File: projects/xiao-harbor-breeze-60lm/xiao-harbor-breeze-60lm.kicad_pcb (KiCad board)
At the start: 2 copper layers, 27.2 x 44.5 mm, 17 parts, among them CN1 XY122V-5.08-2P, CN2 XY122V-5.08-2P, J1 1165SDIG-07, J2 1165SDIG-07, U1 BQ25185DLHR, U2 ME6210A33PG

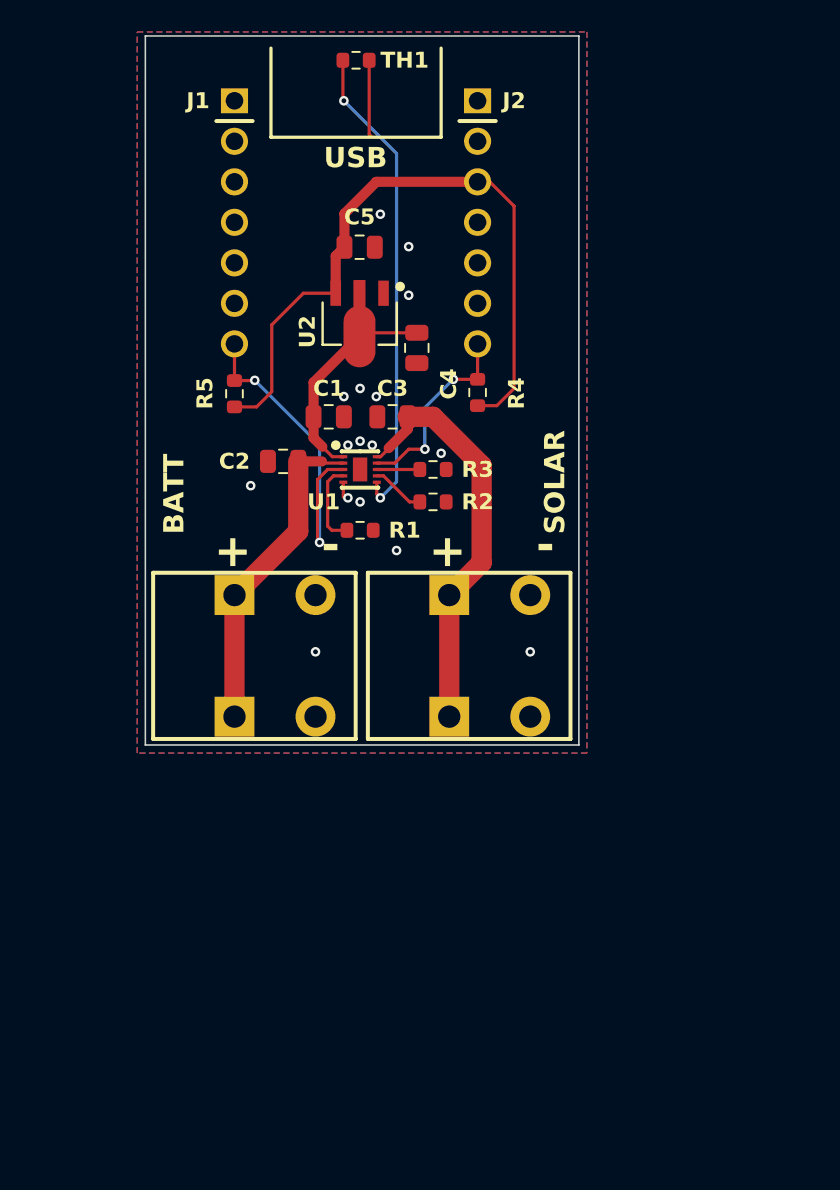
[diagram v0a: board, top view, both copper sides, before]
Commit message: Add low voltage and over voltage protection
This part is a final safety net for battery charage management.

It is configured to have a low voltage cutoff of 2.5V and an over
voltage cutoff of 4.3V.

These values are comfortably outside the range of the change controller
thresholds, but still within the ranges generally accepted to avoid
permanent cell damage.

If for some reason we over charge or over discharge, this part will do a
low side disconnect of the battery from the rest of the system.

lib: Add simple logos

Currently unused, but are available.

See:
  * https://meshtastic.org/docs/legal/licensing-and-trademark/#community-project-logos-m-powered--m-pwrd
  * https://oshwa.org/resources/open-source-hardware-logo/
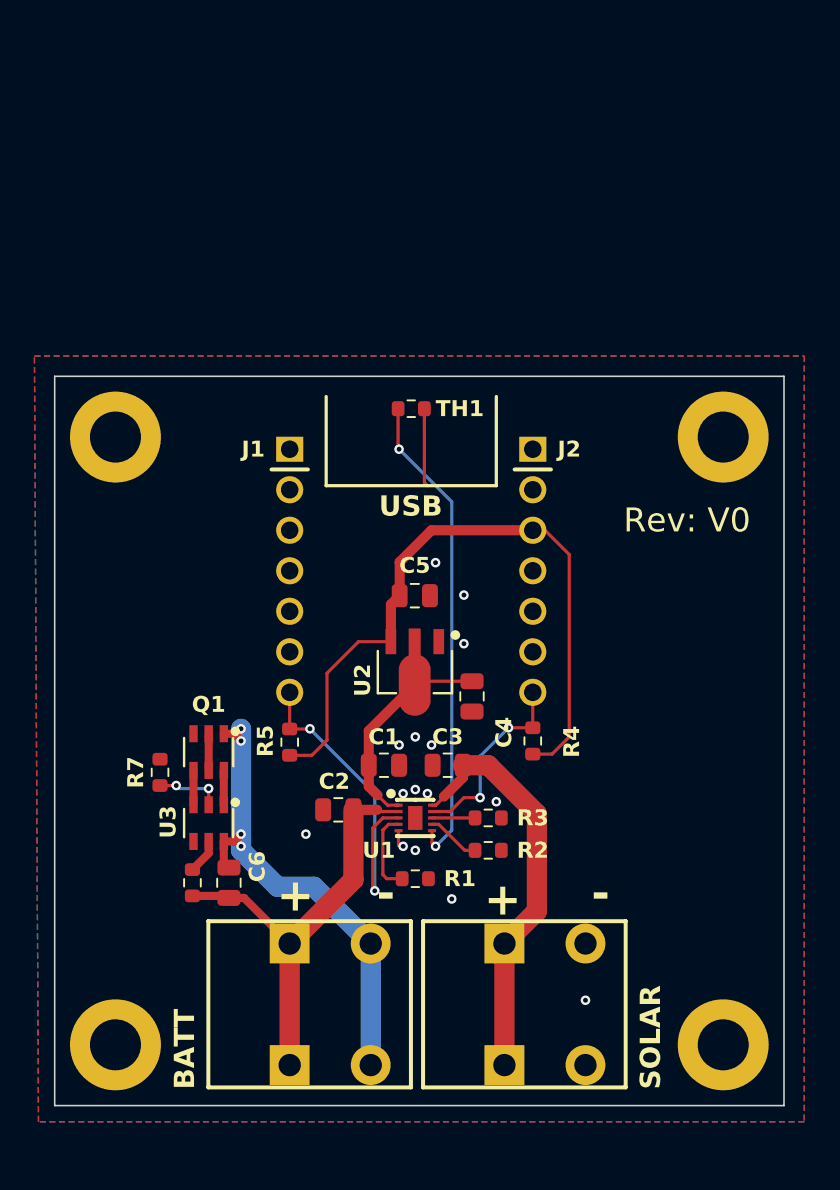
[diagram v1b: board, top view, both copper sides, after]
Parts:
- added C6: 22uF, Capacitor_SMD:C_0805_2012Metric, F.Cu at (136.8, 104.9)
- added H1: MountingHole_Pad, MountingHole:MountingHole_3.2mm_M3_ISO7380_Pad, F.Cu at (167.8, 115.1)
- added H2: MountingHole_Pad, MountingHole:MountingHole_3.2mm_M3_ISO7380_Pad, F.Cu at (129.7, 115.1)
- added H3: MountingHole_Pad, MountingHole:MountingHole_3.2mm_M3_ISO7380_Pad, F.Cu at (167.8, 77.0)
- added H4: MountingHole_Pad, MountingHole:MountingHole_3.2mm_M3_ISO7380_Pad, F.Cu at (129.7, 77.0)
- added Q1: UMW8205A, easyeda2kicad:SOT-23-6_L2.9-W1.6-P0.95-LS2.8-BL, F.Cu at (135.5, 96.7)
- added R6: 100, Resistor_SMD:R_0603_1608Metric, F.Cu at (134.5, 104.9)
- added R7: 1K, Resistor_SMD:R_0603_1608Metric, F.Cu at (132.5, 98.0)
- added U3: DW01A_C351410, easyeda2kicad:SOT-23-6_L2.9-W1.6-P0.95-LS2.8-BL, F.Cu at (135.5, 101.2)
- moved CN2 22.1 mm to (143.2, 112.5)
- moved C1 22.1 mm to (146.5, 97.5)
- moved C3 22.1 mm to (150.5, 97.5)
- moved C4 22.1 mm to (152.1, 93.2)
- moved CN1 22.1 mm to (156.6, 112.5)
- moved R2 22.1 mm to (153.1, 102.9)
- moved C2 22.1 mm to (143.7, 100.3)
- moved C5 22.1 mm to (148.5, 86.9)
- moved J1 22.1 mm to (140.6, 85.3)
- moved J2 22.1 mm to (155.9, 85.3)
- moved R1 22.1 mm to (148.5, 104.6)
- moved R3 22.1 mm to (153.1, 100.8)
- moved R4 22.1 mm to (155.9, 96.0)
- moved R5 22.1 mm to (140.6, 96.1)
- moved TH1 22.1 mm to (148.2, 75.2)
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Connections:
- CN2 pad 2: GND -> -BATT
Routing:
- net -BATT: track 0.00 -> 31.5 mm, vias 0 -> 4
- net +BATT: track 20.5 -> 27.9 mm
- net Net-(U3-VM): track 0.00 -> 4.14 mm, vias 0 -> 2
- net Net-(Q1-D1/D2-Pad2): track 0.00 -> 2.30 mm
- net Net-(U3-VCC): track 0.00 -> 2.18 mm
- net Net-(Q1-G2): track 0.00 -> 2.15 mm
- net Net-(Q1-G1): track 0.00 -> 2.15 mm
- net GND: vias 16 -> 15
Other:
- board size 27.2 x 44.5 mm -> 45.7 x 45.7 mm
- board text added: "Rev: V0"
- board text added: "flyovermesh.org"
- board text added: "github.com/kelledge/heliomesh"

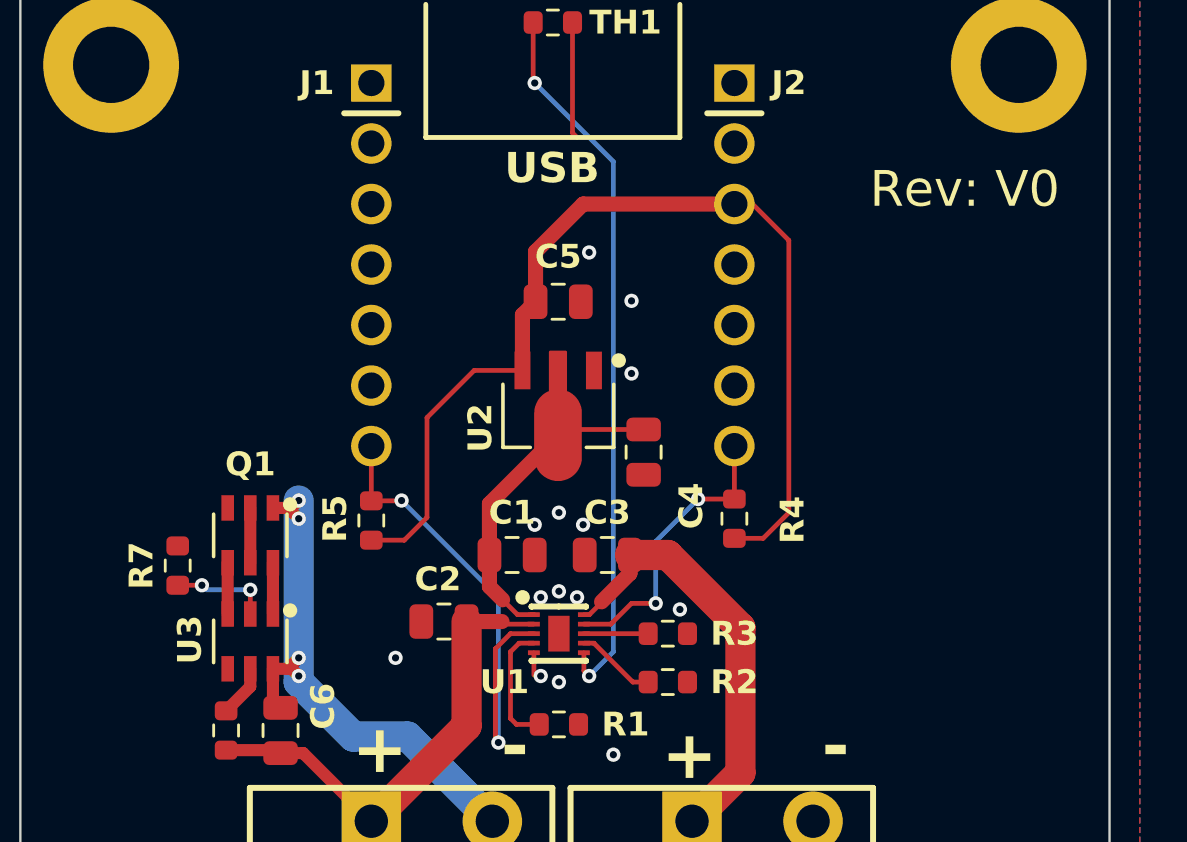
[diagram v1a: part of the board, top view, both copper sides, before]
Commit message: Add ziptie mounting slots
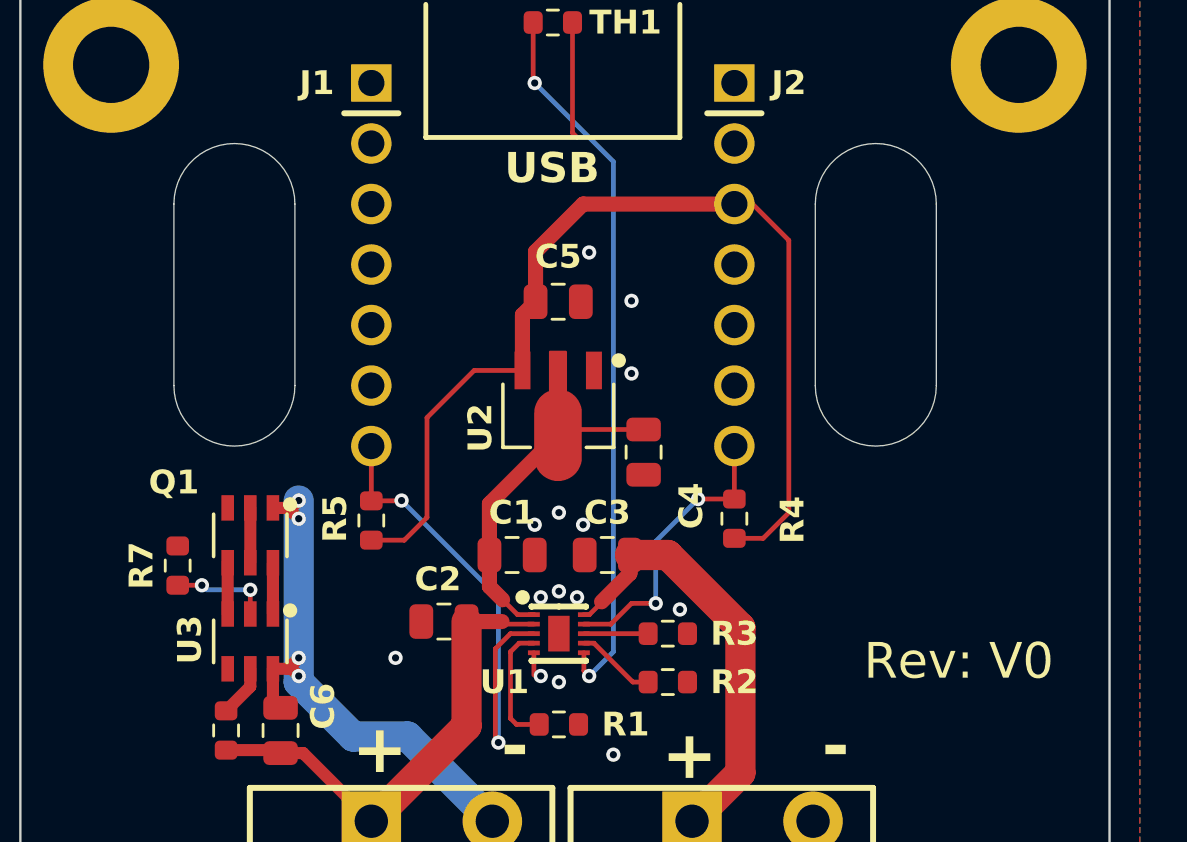
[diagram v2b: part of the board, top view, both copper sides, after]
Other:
- outline, holes or cut-outs redrawn
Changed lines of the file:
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@@
 		(at 135.540862 96.711 180)
 		(property "Reference" "Q1"
-			(at 0 2.985 0)
+			(at 3.206862 2.223 0)
 			(layer "F.SilkS")
 			(effects
@@
 		(layer "F.SilkS")
 	)
+	(gr_line
+		(start 132.334 82.804)
+		(end 132.334 90.424)
+		(stroke
+			(width 0.05)
+			(type default)
+		)
+		(layer "Edge.Cuts")
+	)
+	(gr_line
+		(start 164.338 82.804)
+		(end 164.338 90.424)
+		(stroke
+			(width 0.05)
+			(type default)
+		)
+		(layer "Edge.Cuts")
+	)
+	(gr_arc
+		(start 132.334 82.804)
+		(mid 134.874 80.264)
+		(end 137.414 82.804)
+		(stroke
+			(width 0.05)
+			(type default)
+		)
+		(layer "Edge.Cuts")
+	)
 	(gr_rect
 		(start 125.888862 73.152)
@@
 		(layer "Edge.Cuts")
 	)
+	(gr_arc
+		(start 159.258 82.804)
+		(mid 161.798 80.264)
+		(end 164.338 82.804)
+		(stroke
+			(width 0.05)
+			(type default)
+		)
+		(layer "Edge.Cuts")
+	)
+	(gr_line
+		(start 137.414 82.804)
+		(end 137.414 90.424)
+		(stroke
+			(width 0.05)
+			(type default)
+		)
+		(layer "Edge.Cuts")
+	)
+	(gr_line
+		(start 159.258 82.804)
+		(end 159.258 90.424)
+		(stroke
+			(width 0.05)
+			(type default)
+		)
+		(layer "Edge.Cuts")
+	)
+	(gr_arc
+		(start 137.414 90.424)
+		(mid 134.874 92.964)
+		(end 132.334 90.424)
+		(stroke
+			(width 0.05)
+			(type default)
+		)
+		(layer "Edge.Cuts")
+	)
+	(gr_arc
+		(start 164.338 90.424)
+		(mid 161.798 92.964)
+		(end 159.258 90.424)
+		(stroke
+			(width 0.05)
+			(type default)
+		)
+		(layer "Edge.Cuts")
+	)
 	(gr_text "BATT"
 		(at 134.778862 117.856 90)
@@
 	)
 	(gr_text "Rev: V0"
-		(at 161.544 83.058 0)
+		(at 161.29 102.87 0)
 		(layer "F.SilkS")
 		(effects

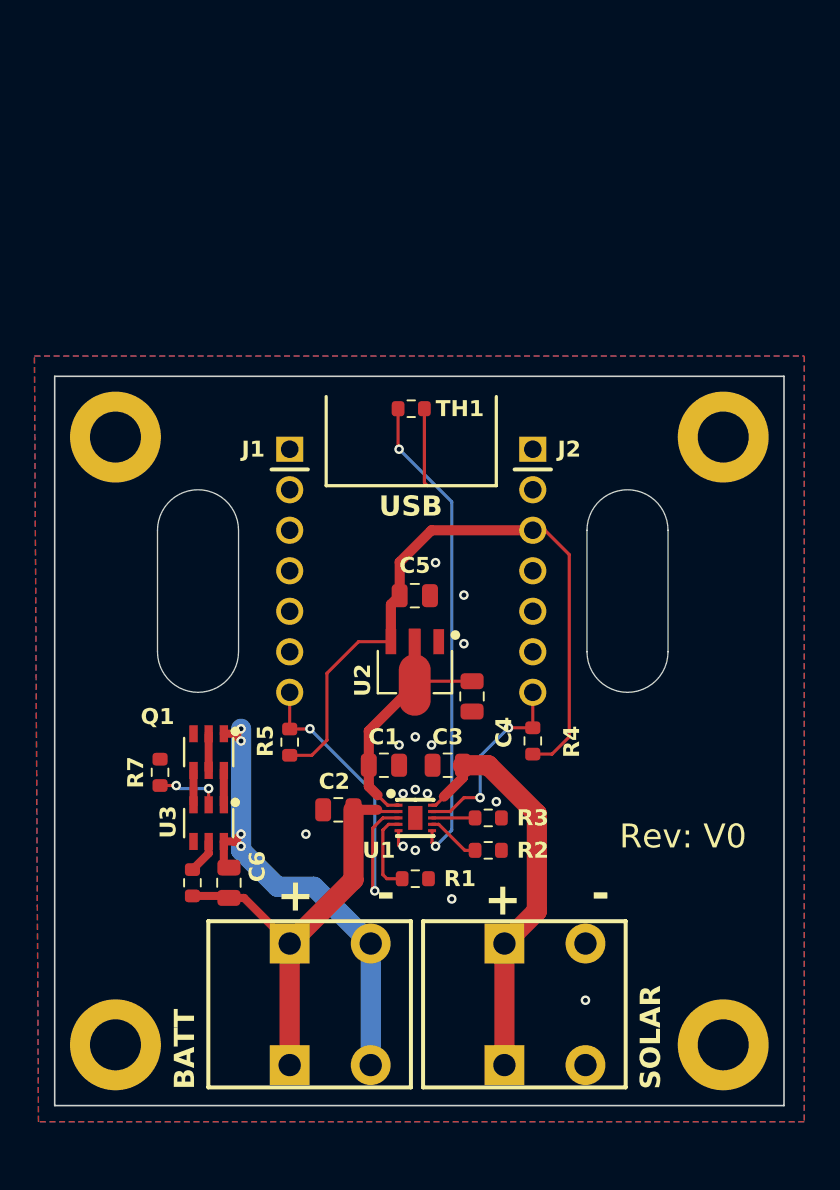
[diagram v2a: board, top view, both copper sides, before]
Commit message: Use horizontally oriented spring terminals
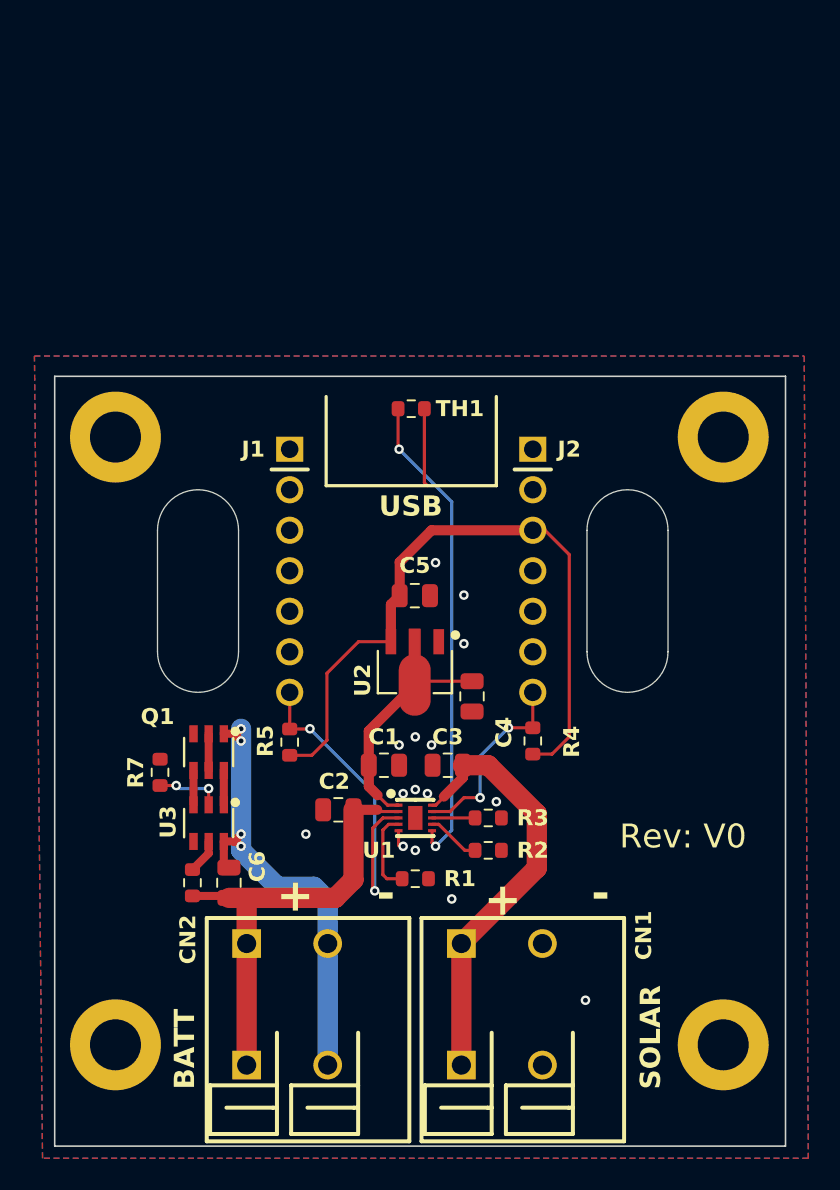
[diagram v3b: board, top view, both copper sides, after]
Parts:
- CN1, CN2: footprint easyeda2kicad:CONN-TH_XY122V-5.08-2P -> easyeda2kicad:CONN-TH_XY122R-5.08-2P
- moved CN2 2.70 mm to (140.5, 112.5)
- moved CN1 2.70 mm to (153.9, 112.5)
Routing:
- net +BATT: track 27.9 -> 29.4 mm
- net VBUS: track 25.6 -> 26.7 mm
- net -BATT: track 31.5 -> 30.4 mm
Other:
- board size 45.7 x 45.7 mm -> 45.8 x 48.3 mm

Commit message: Add test points and status LEDs
LEDs allow simple confirmation of the board state. Cut their traces
after testing to save around 20mW of power draw.

Added test points to important signals to speed up diagnosing any issues
with the initial design.

Minor update to README.md
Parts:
- added D1: FAULT, LED_SMD:LED_0603_1608Metric, F.Cu at (167.9, 100.6)
- added D2: CHARG, LED_SMD:LED_0603_1608Metric, F.Cu at (167.9, 103.9)
- added D3: 3V3, LED_SMD:LED_0603_1608Metric, F.Cu at (168.0, 97.3)
- added G1: ~, heliomesh:mesh_pwrd_very_small, B.Cu at (154.4, 106.5)
- added G2: ~, heliomesh:oshw_very_small, B.Cu at (152.9, 82.9)
- added R10: 100, Resistor_SMD:R_0603_1608Metric, F.Cu at (164.4, 97.3)
- added R8: 100, Resistor_SMD:R_0603_1608Metric, F.Cu at (164.4, 100.6)
- added R9: 100, Resistor_SMD:R_0603_1608Metric, F.Cu at (164.4, 103.9)
- added TP1: TestPoint, TestPoint:TestPoint_Pad_D1.5mm, B.Cu at (148.6, 108.7)
- added TP2: TestPoint, TestPoint:TestPoint_Pad_D1.5mm, B.Cu at (145.5, 92.5)
- added TP3: TestPoint, TestPoint:TestPoint_Pad_D1.5mm, B.Cu at (135.1, 108.7)
- added TP4: TestPoint, TestPoint:TestPoint_Pad_D1.5mm, B.Cu at (164.1, 100.6)
- added TP5: TestPoint, TestPoint:TestPoint_Pad_D1.5mm, B.Cu at (164.1, 103.9)
- added TP6: TestPoint, TestPoint:TestPoint_Pad_D1.5mm, B.Cu at (164.1, 97.3)
- added TP7: TestPoint, TestPoint:TestPoint_Pad_D1.5mm, B.Cu at (131.8, 96.8)
- added TP8: TestPoint, TestPoint:TestPoint_Pad_D1.5mm, B.Cu at (131.8, 101.6)
- added TP9: TestPoint, TestPoint:TestPoint_Pad_D1.5mm, B.Cu at (159.5, 108.7)
- CN1, CN2: value XY122V-5.08-2P -> XY122R-5.08-2P
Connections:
- net Net-(Q1-G1) renamed /OD
- net Net-(Q1-G2) renamed /OC
- net Net-(U3-VM) renamed /VM
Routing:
- net /STAT2: track 21.3 -> 47.1 mm, vias 2 -> 3
- net +3V3: track 43.2 -> 63.3 mm, vias 0 -> 1
- net /STAT1: track 12.2 -> 31.3 mm, vias 2 -> 3
- net /OD: track 2.15 -> 7.47 mm, vias 0 -> 1
- net /OC: track 2.15 -> 5.37 mm, vias 0 -> 1
- net VCC: track 13.7 -> 16.5 mm, vias 0 -> 1
- net +BATT: track 29.4 -> 32.2 mm
- net VBUS: track 26.7 -> 29.5 mm
- net Net-(D3-A): track 0.00 -> 1.94 mm
- net Net-(D2-A): track 0.00 -> 1.91 mm
- net Net-(D1-A): track 0.00 -> 1.91 mm
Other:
- board text added: "3V3"
- board text added: "CHRG"
- board text added: "FAULT"
